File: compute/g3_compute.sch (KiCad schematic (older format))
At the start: 37 parts, among them J101 CONSMA001-SMD-G, J102 Temp_Connector_1x4, J103 Conn_02x03_Counter_Clockwise, J104 Conn_Power_Compute_02x05, J105 GPIO_Breakout_Conn, U101 PA1616D, U102 LoRa-E5

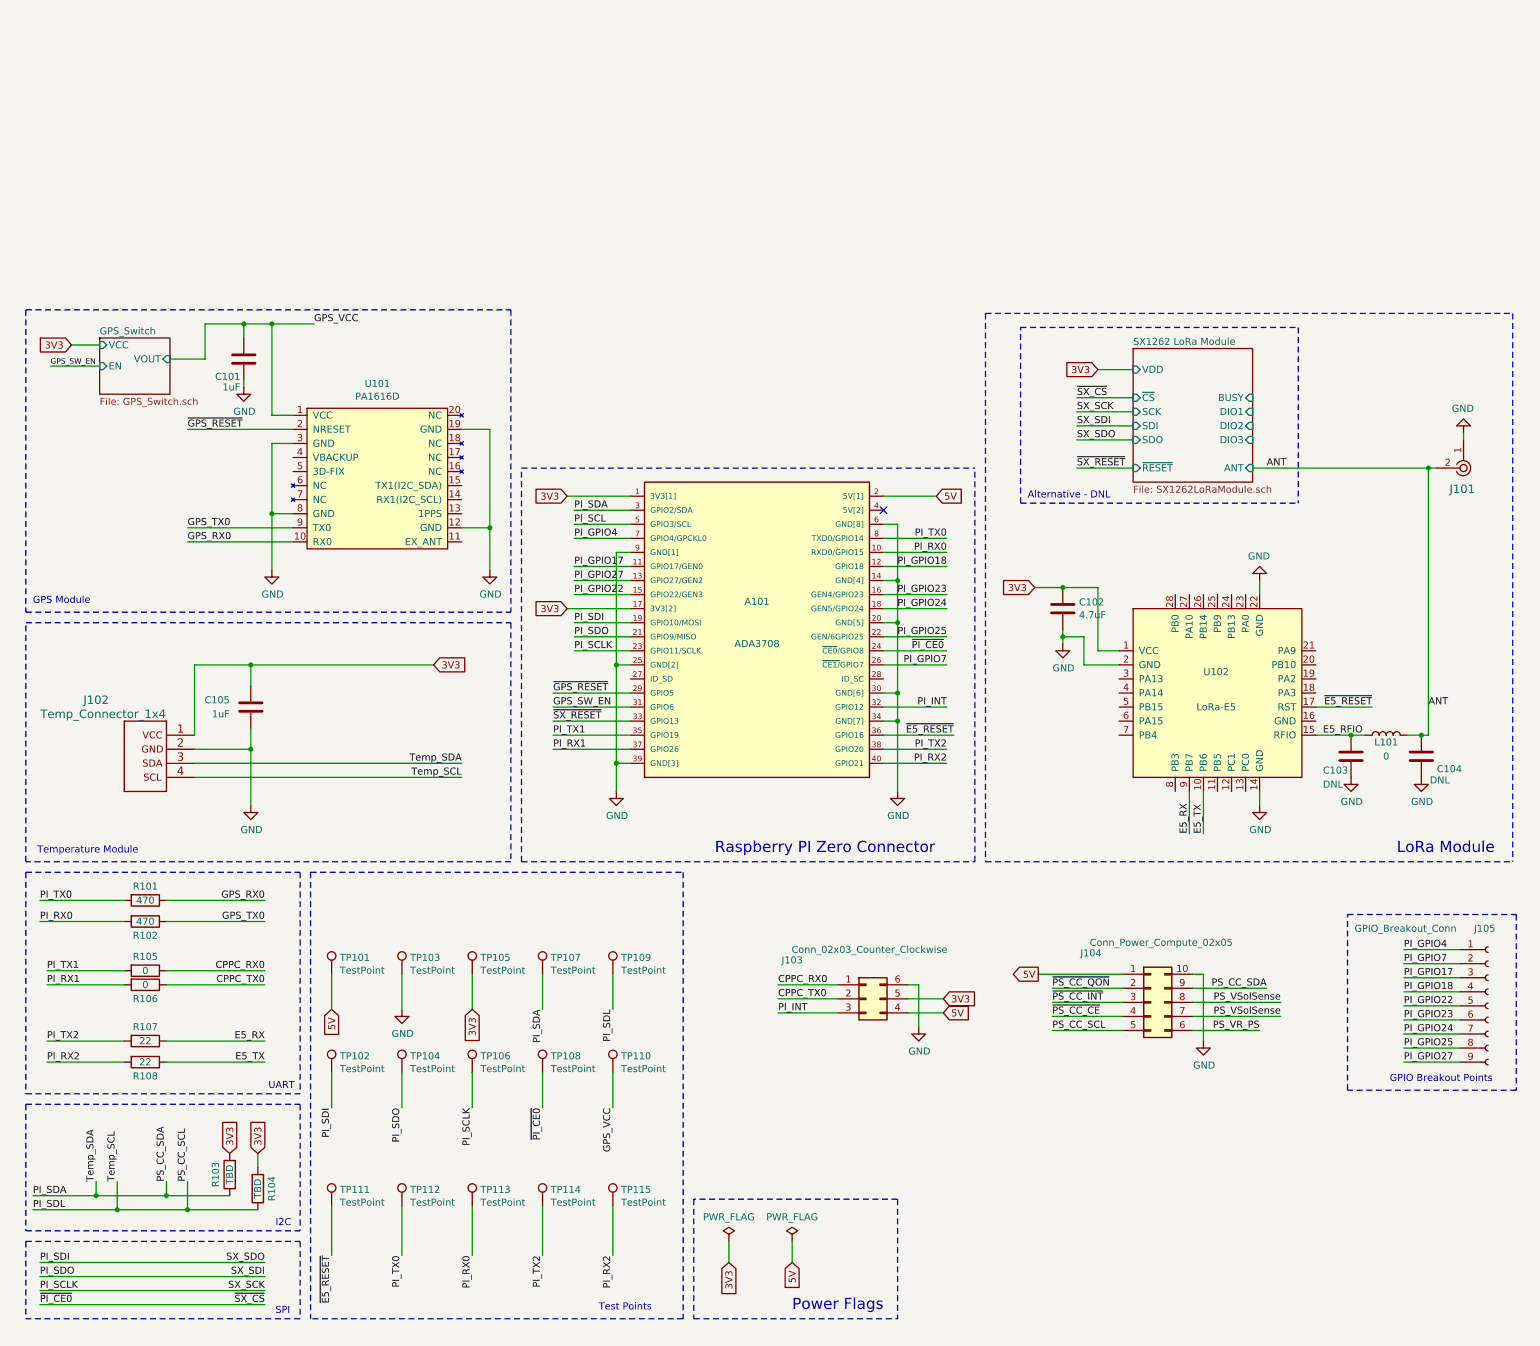
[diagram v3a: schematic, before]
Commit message: Mapping Power systems signals to pi
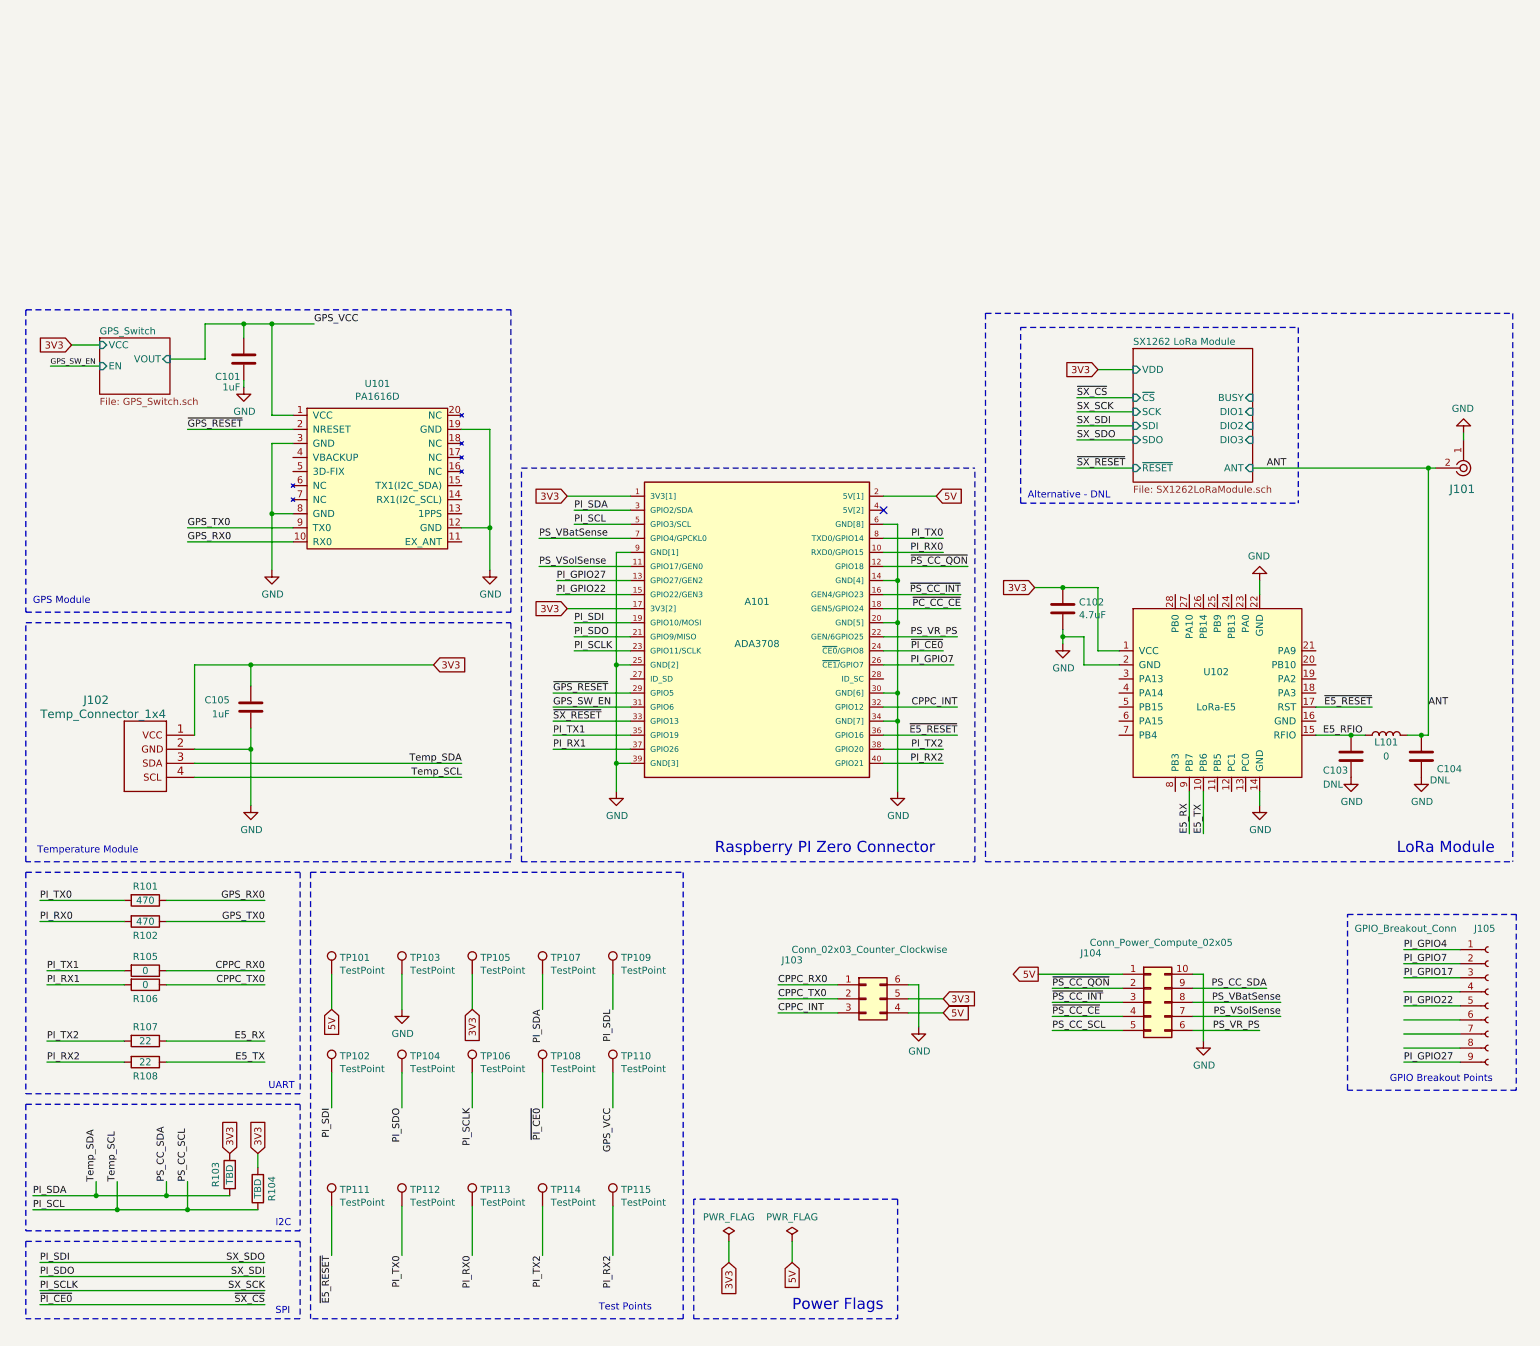
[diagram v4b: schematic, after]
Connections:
- net PI_GPIO17: no longer A101.11 (GPIO17/GEN0)
- net PI_GPIO4: no longer A101.7 (GPIO4/GPCKL0)
- net PI_SCL: now also J102.4 (SCL), J104.5 (Pin_5), R104.1
- net PI_SDL: no longer J102.4 (SCL), J104.5 (Pin_5), R104.1
- net PS_VR_PS: now also A101.22 (GEN/6GPIO25)
- net PS_VSolSense: now also A101.11 (GPIO17/GEN0); no longer J104.8 (Pin_8)
- net ~PS_CC_INT: now also A101.16 (GEN4/GPIO23)
- net ~PS_CC_QON: now also A101.12 (GPIO18)
- net PI_GPIO18: no longer names the net of J105.4 (Pin_4)
- net PI_GPIO18: no longer A101.12 (GPIO18)
- net PI_GPIO23: no longer names the net of J105.6 (Pin_6)
- net PI_GPIO23: no longer A101.16 (GEN4/GPIO23)
- net PI_GPIO24: no longer names the net of J105.7 (Pin_7)
- net PI_GPIO24: no longer A101.18 (GEN5/GPIO24)
- net PI_GPIO25: no longer names the net of J105.8 (Pin_8)
- net PI_GPIO25: no longer A101.22 (GEN/6GPIO25)
- net PI_INT renamed CPPC_INT
- new net PS_VBatSense: A101.7 (GPIO4/GPCKL0), J104.8 (Pin_8)
- new net ~PC_CC_CE: A101.18 (GEN5/GPIO24)
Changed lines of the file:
@@
 	1    0    0    -1
 $EndComp
-Text Label 3650 3775 2    50   ~ 0
-Temp_SDA
-Text Label 3650 3875 2    50   ~ 0
-Temp_SCL
 Wire Notes Line
 	550  2775 4000 2775
@@
 Text GLabel 7025 1875 2    50   Input ~ 0
 5V
-Text Label 6850 2975 0    50   ~ 0
+Text Label 7075 2975 2    50   ~ 0
 ~PI_CE0
 Text Label 4450 2875 0    50   ~ 0
@@
 PI_SDA
 Text Label 600  6950 0    50   ~ 0
-PI_SDL
-Text Label 7100 2175 2    50   ~ 0
+PI_SCL
+Text Label 7075 2175 2    50   ~ 0
 PI_TX0
-Text Label 7100 2275 2    50   ~ 0
+Text Label 7075 2275 2    50   ~ 0
 PI_RX0
 Wire Wire Line
-	6650 2175 7100 2175
-Wire Wire Line
-	6650 2275 7100 2275
+	6650 2175 7075 2175
+Wire Wire Line
+	6650 2275 7075 2275
 Text Label 1050 6750 1    50   ~ 0
 Temp_SDA
@@
 	550  6200 2500 6200
 Wire Wire Line
-	6650 2975 7100 2975
+	6650 2975 7075 2975
 Text Notes 2275 6100 0    50   ~ 0
 UART
@@
 Wire Wire Line
 	2150 3075 3450 3075
-Wire Wire Line
-	1750 3875 3650 3875
-Wire Wire Line
-	1750 3775 3650 3775
 Text GLabel 2000 6550 1    50   Input ~ 0
 3V3
@@
 	4850 3675 4300 3675
 Wire Wire Line
-	6650 3675 7100 3675
-Wire Wire Line
-	6650 3775 7100 3775
+	6650 3675 7075 3675
+Wire Wire Line
+	6650 3775 7075 3775
 Text Label 700  5900 0    50   ~ 0
 PI_RX2
@@
 Text Label 4300 3675 0    50   ~ 0
 PI_RX1
-Text Label 7100 3675 2    50   ~ 0
+Text Label 7075 3675 2    50   ~ 0
 PI_TX2
-Text Label 7100 3775 2    50   ~ 0
+Text Label 7075 3775 2    50   ~ 0
 PI_RX2
 $Comp
@@
 Wire Wire Line
 	1550 5900 2250 5900
-Text Label 7150 3575 2    50   ~ 0
+Text Label 7175 3575 2    50   ~ 0
 ~E5_RESET
 Wire Wire Line
-	6650 3575 7150 3575
+	6650 3575 7175 3575
 Wire Wire Line
 	4725 5975 4725 6225
@@
 PI_RX2
 Wire Wire Line
-	4850 2575 4450 2575
-Wire Wire Line
-	4850 2475 4450 2475
-Wire Wire Line
-	4850 2375 4450 2375
-Wire Wire Line
-	4850 2175 4450 2175
-Wire Wire Line
-	6650 2375 7100 2375
-Wire Wire Line
-	6650 2575 7100 2575
-Wire Wire Line
-	6650 2675 7100 2675
-Wire Wire Line
-	6650 2875 7100 2875
-Wire Wire Line
-	6650 3075 7100 3075
-Wire Wire Line
-	6650 3375 7100 3375
-Text Label 4450 2175 0    50   ~ 0
-PI_GPIO4
-Text Label 4450 2375 0    50   ~ 0
-PI_GPIO17
-Text Label 4450 2475 0    50   ~ 0
+	4850 2575 4325 2575
+Wire Wire Line
+	4850 2475 4325 2475
+Wire Wire Line
+	4850 2375 4200 2375
+Wire Wire Line
+	4850 2175 4200 2175
+Wire Wire Line
+	6650 2375 7250 2375
+Wire Wire Line
+	6650 2575 7200 2575
+Wire Wire Line
+	6650 2675 7200 2675
+Wire Wire Line
+	6650 2875 7175 2875
+Wire Wire Line
+	6650 3075 7150 3075
+Wire Wire Line
+	6650 3375 7175 3375
+Text Label 4200 2175 0    50   ~ 0
+PS_VBatSense
+Text Label 4200 2375 0    50   ~ 0
+PS_VSolSense
+Text Label 4325 2475 0    50   ~ 0
 PI_GPIO27
-Text Label 4450 2575 0    50   ~ 0
+Text Label 4325 2575 0    50   ~ 0
 PI_GPIO22
-Text Label 7100 2375 2    50   ~ 0
-PI_GPIO18
-Text Label 7100 2575 2    50   ~ 0
-PI_GPIO23
-Text Label 7100 2675 2    50   ~ 0
-PI_GPIO24
-Text Label 7100 2875 2    50   ~ 0
-PI_GPIO25
-Text Label 7100 3075 2    50   ~ 0
+Text Label 7250 2375 2    50   ~ 0
+~PS_CC_QON
+Text Label 7200 2575 2    50   ~ 0
+~PS_CC_INT
+Text Label 7200 2675 2    50   ~ 0
+~PC_CC_CE
+Text Label 7175 2875 2    50   ~ 0
+PS_VR_PS
+Text Label 7150 3075 2    50   ~ 0
 PI_GPIO7
-Text Label 7100 3375 2    50   ~ 0
-PI_INT
+Text Label 7175 3375 2    50   ~ 0
+CPPC_INT
 Text Notes 4625 7675 0    50   ~ 0
 Test Points
@@
 CPPC_TX0
 Text Label 5900 5550 0    50   ~ 0
-PI_INT
+CPPC_INT
 Text GLabel 7075 5550 2    50   Input ~ 0
 5V
@@
 Text Label 10350 5500 0    50   ~ 0
 PI_GPIO22
-Text Label 10350 5400 0    50   ~ 0
-PI_GPIO18
-Text Label 10350 5600 0    50   ~ 0
-PI_GPIO23
-Text Label 10350 5700 0    50   ~ 0
-PI_GPIO24
-Text Label 10350 5800 0    50   ~ 0
-PI_GPIO25
 Text Label 10350 5200 0    50   ~ 0
 PI_GPIO7
@@
 Wire Wire Line
 	7750 5275 8350 5275
-Text Label 9475 5475 2    50   ~ 0
-PS_VSolSense
 Text Label 9475 5575 2    50   ~ 0
 PS_VSolSense
@@
 Wire Wire Line
 	10525 1675 10575 1675
+Text Label 9475 5475 2    50   ~ 0
+PS_VBatSense
+Wire Wire Line
+	1750 3775 3650 3775
+Wire Wire Line
+	1750 3875 3650 3875
+Text Label 3650 3875 2    50   ~ 0
+Temp_SCL
+Text Label 3650 3775 2    50   ~ 0
+Temp_SDA
 $EndSCHEMATC

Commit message: changes to compute
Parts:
- removed TP110: TestPoint, Capacitor_SMD:C_0805_2012Metric_Pad1.18x1.45mm_HandSolder, symbol Connector:TestPoint
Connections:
- net labels added: +3.3V, +5V
- net labels removed: 3V3, 5V, GPS_VCC, PI_SDL, SX_SCK, SX_SDI, SX_SDO, ~SX_CS
- wire segments 175 -> 161
- no-connect marks 1 -> 19
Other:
- note removed: "SPI"
- moved on the sheet: C102, C103, C104, L101, R104, TP101, TP102, TP103, TP104, TP105, TP106, TP107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

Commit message: fixes to power and compute
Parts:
- removed J103: Conn_02x03_Counter_Clockwise, Connector_Samtec_HLE_SMD:Samtec_HLE-103-02-xxx-DV_2x03_P2.54mm_Horizontal, symbol Connector_Generic:Conn_02x03_Counter_Clockwise
- removed J104: Conn_Power_Compute_02x05, Connector_Samtec_HLE_SMD:Samtec_HLE-105-02-xxx-DV_2x05_P2.54mm_Horizontal, symbol Connector_Generic:Conn_02x05_Counter_Clockwise
- removed J105: GPIO_Breakout_Conn, Connector_Samtec_HLE_SMD:Samtec_HLE-105-02-xxx-DV_2x05_P2.54mm_Horizontal, symbol Connector:Conn_01x09_Female
- added J1, J2: Conn_01x10_Female, Connector_Molex:Molex_CLIK-Mate_502386-1070_1x10-1MP_P1.25mm_Horizontal, symbol Connector:Conn_01x10_Female
- added TP1, TP2, TP3: TestPoint, Capacitor_SMD:C_0805_2012Metric_Pad1.18x1.45mm_HandSolder, symbol Connector:TestPoint
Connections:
- net labels removed: PI_GPIO17, PI_GPIO4
- wire segments 161 -> 162
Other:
- note removed: "Alternative - DNL"
- note removed: "GPIO Breakout Points"

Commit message: adding footprints
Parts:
- J1, J2: footprint Connector_Molex:Molex_CLIK-Mate_502386-1070_1x10-1MP_P1.25mm_Horizontal -> Perch:532611071_Molex
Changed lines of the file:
@@
 F 0 "J1" H 7953 5126 50  0000 L CNN
 F 1 "Conn_01x10_Female" H 7250 5675 50  0000 L CNN
-F 2 "Connector_Molex:Molex_CLIK-Mate_502386-1070_1x10-1MP_P1.25mm_Horizontal" H 7925 5150 50  0001 C CNN
+F 2 "Perch:532611071_Molex" H 7925 5150 50  0001 C CNN
 F 3 "~" H 7925 5150 50  0001 C CNN
 	1    7925 5150
@@
 F 0 "J2" H 9778 5226 50  0000 L CNN
 F 1 "Conn_01x10_Female" H 9025 5775 50  0000 L CNN
-F 2 "Connector_Molex:Molex_CLIK-Mate_502386-1070_1x10-1MP_P1.25mm_Horizontal" H 9750 5250 50  0001 C CNN
+F 2 "Perch:532611071_Molex" H 9750 5250 50  0001 C CNN
 F 3 "~" H 9750 5250 50  0001 C CNN
 	1    9750 5250
@@
 	2275 6425 2275 6525
 $Comp
-L power:+5V #PWR?
+L power:+5V #PWR0122
 U 1 1 61DC6E6C
 P 8950 4850
-F 0 "#PWR?" H 8950 4700 50  0001 C CNN
+F 0 "#PWR0122" H 8950 4700 50  0001 C CNN
 F 1 "+5V" V 8965 5023 50  0000 C CNN
 F 2 "" H 8950 4850 50  0001 C CNN

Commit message: Making changes suggested
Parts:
- added J?: 53261-1071, 532611071, symbol 53261-1071:53261-1071
- R103, R104: value TBD -> 10k
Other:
- note added: "Note: \nProbably used as filters, do \nnot load until needed"
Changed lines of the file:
@@
 P 2000 6700
 F 0 "R103" V 2100 6700 50  0000 C CNN
-F 1 "TBD" V 2000 6700 50  0000 C CNN
+F 1 "10k" V 2000 6700 50  0000 C CNN
 F 2 "Resistor_SMD:R_0402_1005Metric_Pad0.72x0.64mm_HandSolder" V 1930 6700 50  0001 C CNN
 F 3 "~" H 2000 6700 50  0001 C CNN
@@
 P 2275 6800
 F 0 "R104" V 2175 6800 50  0000 C CNN
-F 1 "TBD" V 2275 6800 50  0000 C CNN
+F 1 "10k" V 2275 6800 50  0000 C CNN
 F 2 "Resistor_SMD:R_0402_1005Metric_Pad0.72x0.64mm_HandSolder" V 2205 6800 50  0001 C CNN
 F 3 "~" H 2275 6800 50  0001 C CNN
@@
 Wire Wire Line
 	8925 5650 9550 5650
+$Comp
+L 53261-1071:53261-1071 J?
+U 1 1 61E456C4
+P 10900 4825
+F 0 "J?" H 11350 5090 50  0000 C CNN
+F 1 "53261-1071" H 11350 4999 50  0000 C CNN
+F 2 "532611071" H 11650 4925 50  0001 L CNN
+F 3 "https://www.molex.com/webdocs/datasheets/pdf/en-us/0532611071_PCB_HEADERS.pdf" H 11650 4825 50  0001 L CNN
+F 4 "10 way SMT r/a header Molex PICOBLADE Series, Series Number 53261, 1.25mm Pitch 10 Way 1 Row Shrouded Right Angle PCB Header, Surface Mount" H 11650 4725 50  0001 L CNN "Description"
+F 5 "3" H 11650 4625 50  0001 L CNN "Height"
+F 6 "538-53261-1071" H 11650 4525 50  0001 L CNN "Mouser Part Number"
+F 7 "https://www.mouser.co.uk/ProductDetail/Molex/53261-1071?qs=%252B72YyncTwW%252Bzs3RwZTiukQ%3D%3D" H 11650 4425 50  0001 L CNN "Mouser Price/Stock"
+F 8 "Molex" H 11650 4325 50  0001 L CNN "Manufacturer_Name"
+F 9 "53261-1071" H 11650 4225 50  0001 L CNN "Manufacturer_Part_Number"
+	1    10900 4825
+	-1   0    0    -1
+$EndComp
+Text Notes 9775 3225 0    50   ~ 0
+Note: \nProbably used as filters, do \nnot load until needed
 $EndSCHEMATC
